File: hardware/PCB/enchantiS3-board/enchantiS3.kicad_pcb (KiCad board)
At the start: 4 copper layers, 55.9 x 25.4 mm, 66 parts, among them J1 USB_C_Receptacle_USB2.0, Q1 BSS138, Q2 BSS138, Q3 BSS138, SW1 B3U-1000P, SW2 B3U-1000P, U1 USBLC6-2P6, U2 MCP73871, U3 NCP167AMX330TBG, U4 NCP167AMX180TBG

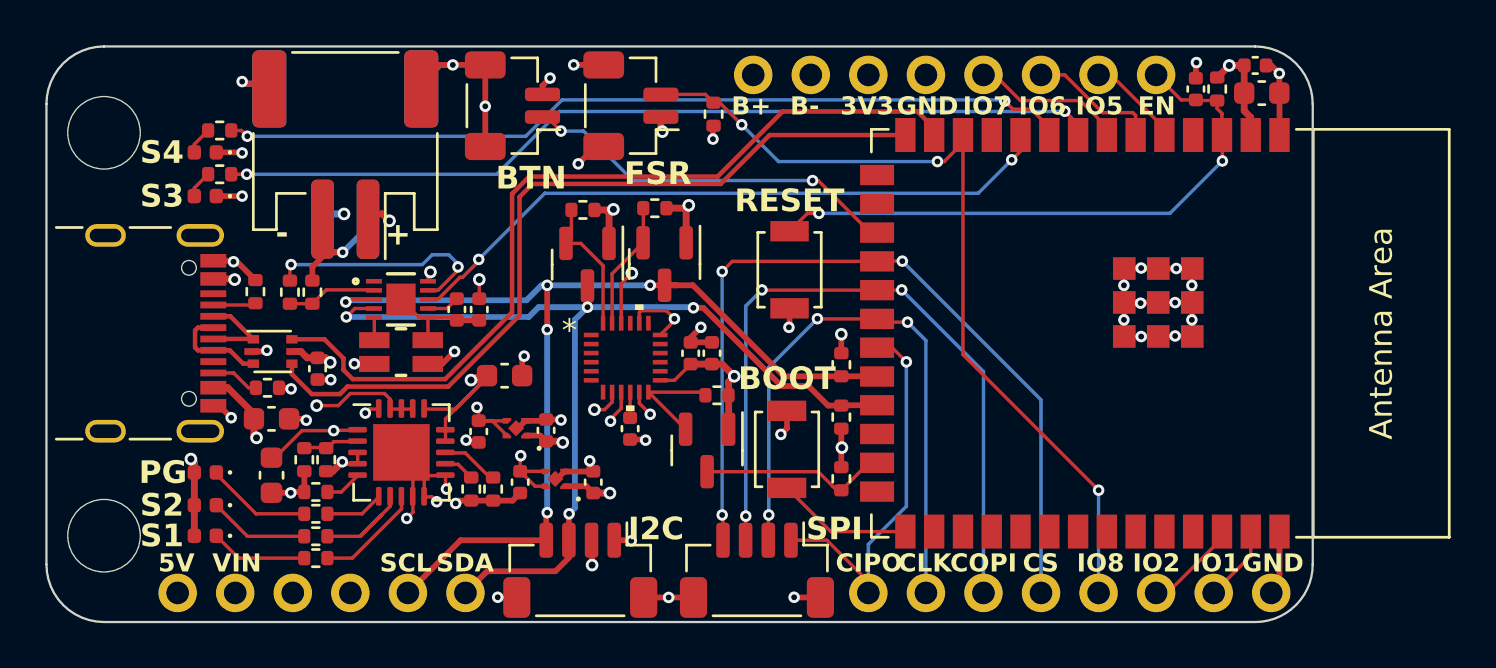
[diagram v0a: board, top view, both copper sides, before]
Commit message: removed, neopixel library, added extra LDO for peripherals
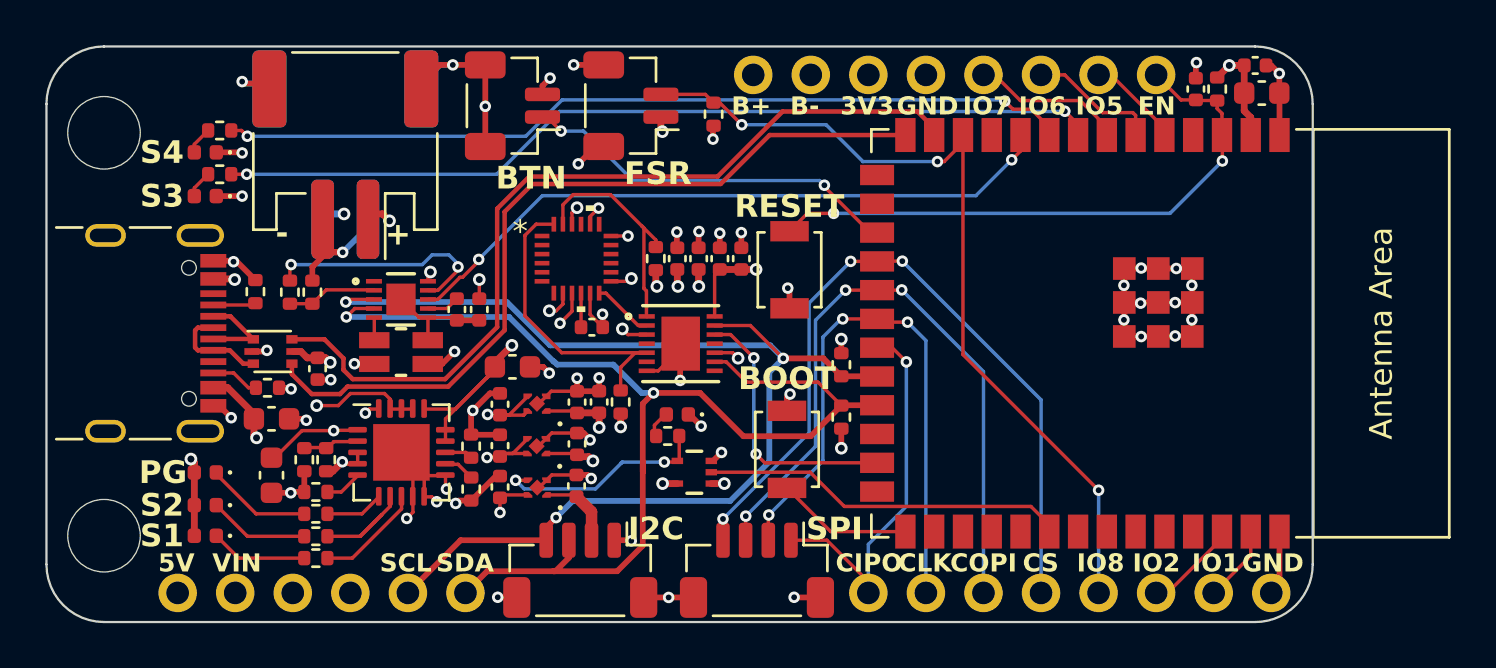
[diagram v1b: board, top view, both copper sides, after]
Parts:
- removed Q1, Q2, Q3: BSS138, Package_TO_SOT_SMD:SOT-23
- removed R21, R23: 2k2, Resistor_SMD:R_0402_1005Metric
- added C16: 1uF, Capacitor_SMD:C_0402_1005Metric, F.Cu at (116.1, 67.7)
- added C17: 1uF, Capacitor_SMD:C_0402_1005Metric, F.Cu at (112.7, 65.9)
- added C18: 0.1uF, Capacitor_SMD:C_0402_1005Metric, F.Cu at (117.1, 64.0)
- added C20: 1uF, Capacitor_SMD:C_0402_1005Metric, F.Cu at (122.4, 57.6)
- added C21: 0.1uF, Capacitor_SMD:C_0402_1005Metric, F.Cu at (123.4, 57.6)
- added LDOLED1: LDO2LED, LED_SMD:LED_0402_1005Metric, F.Cu at (120.5, 64.5)
- added R11: 1k, Resistor_SMD:R_0402_1005Metric, F.Cu at (120.1, 65.5)
- added U5: NCP167AMX330TBG, NCP167AMX330TBG-footprints:XDFN4_1X1_711AJ_ONS, F.Cu at (114.4, 67.7)
- added U6: NL17SV08XV5T2G, NL17SV08-footprints:SOT553-5_ONS, F.Cu at (121.3, 67.0)
- added U7: max3378eetd+t, MAX3378E-footprints:21-0137I_T1433-2_MXM, F.Cu at (120.7, 61.4)
- moved R15 8.64 mm to (118.0, 64.0), turned to -90 degrees
- moved IMU1 4.88 mm to (116.1, 57.6)
- moved C6 4.78 mm to (116.8, 60.6), turned to 0 degrees
- moved C10 4.22 mm to (121.5, 57.6)
- moved C7 4.22 mm to (120.5, 57.6)
- moved R14 2.23 mm to (119.6, 57.6), turned to -90 degrees
- moved R20 2.13 mm to (111.5, 65.9), turned to -90 degrees
- moved C12 1.85 mm to (116.1, 64.0)
- moved C5 1.83 mm to (116.1, 65.8)
- moved U3 1.66 mm to (114.3, 65.9)
- moved C11 1.53 mm to (112.7, 64.0), turned to 90 degrees
- moved U4 1.42 mm to (114.4, 64.0)
- moved C4 0.91 mm to (112.7, 67.7), turned to 90 degrees
- moved C8 0.52 mm to (113.3, 62.4)
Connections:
- TOUCH1 pad 2: +3V3 -> +3V3_AUX
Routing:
- net /IO39: track 0.00 -> 16.2 mm
- net GND: track 80.4 -> 92.3 mm, vias 48 -> 56
- net /LDO_EN: track 0.00 -> 9.56 mm, vias 0 -> 2
- net /SCL: track 45.6 -> 53.2 mm, vias 5 -> 3
- net /SDA: track 44.3 -> 51.7 mm, vias 4 -> 2
- net /LV_SDA: track 6.16 -> 13.5 mm
- net +1V8: track 16.9 -> 11.2 mm, vias 6 -> 10
- net /LV_SCL: track 5.64 -> 10.4 mm
- net /IO48: track 8.34 -> 11.9 mm, vias 0 -> 2
- net +3V3_AUX: track 0.00 -> 3.55 mm
- net /CS: track 37.2 -> 34.1 mm
- net +3V3: track 11.1 -> 14.0 mm, vias 6 -> 8
- net /IMU_INT: track 4.89 -> 2.69 mm
- net /COPI: track 32.4 -> 30.2 mm
- net SYS: track 11.3 -> 13.0 mm, vias 4 -> 5
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
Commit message: updated schematic
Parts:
- removed LDOLED1: LDO2LED, LED_SMD:LED_0402_1005Metric
- removed R11: 1k, Resistor_SMD:R_0402_1005Metric
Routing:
- net /SDA: track 51.7 -> 50.4 mm
- net /LDO_EN: track 9.56 -> 8.33 mm
- net Net-(LDOLED1-A): track 1.22 -> 0.00 mm
- net GND: track 92.3 -> 91.5 mm, vias 56 -> 55

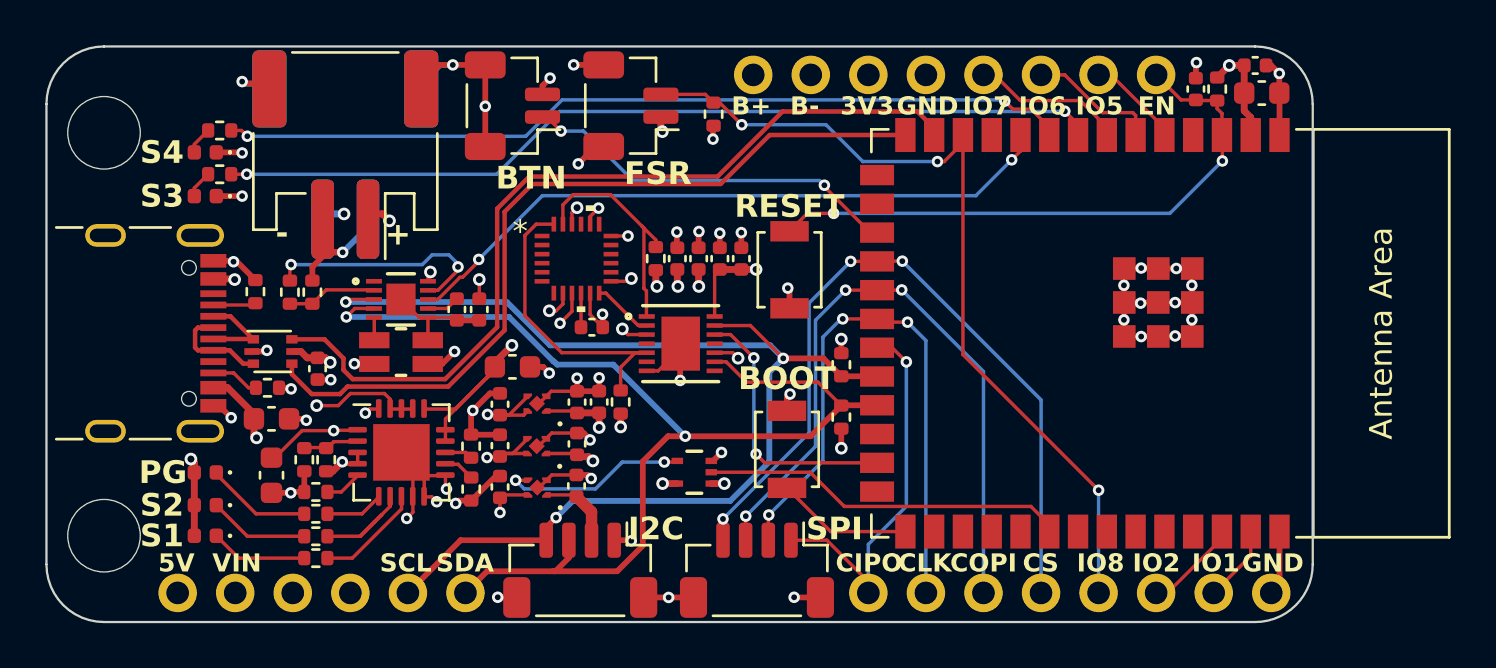
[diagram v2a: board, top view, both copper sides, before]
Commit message: upadated schematic, connected IMU data pins to SPI line, updated manufacturing files
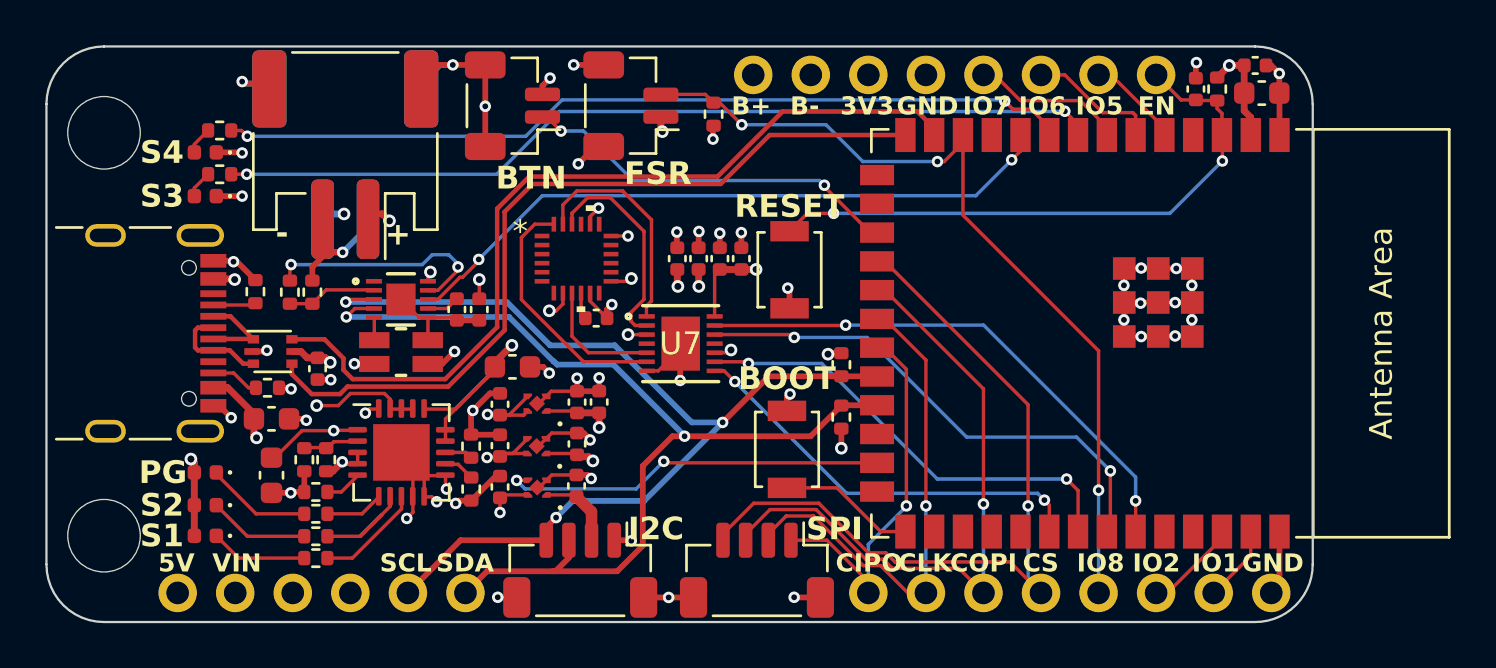
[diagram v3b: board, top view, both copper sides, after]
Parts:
- removed R14, R15: 2k2, Resistor_SMD:R_0402_1005Metric
- removed U6: NL17SV08XV5T2G, NL17SV08-footprints:SOT553-5_ONS
- moved C6 0.44 mm to (117.0, 60.2)
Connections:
- net /LV_SCL renamed /CLK_1V8
- IMU1 pad 12: /IMU_INT -> unconnected-(IMU1-INT1-Pad12)
- IMU1 pad 22: +1V8 -> /CS_1V8
- IMU1 pad 24: /LV_SDA -> /COPI_1V8
- IMU1 pad 9: GND -> /CIPO_1V8
- MCU1 pad 25: /IO48 -> /LDO_EN
- MCU1 pad 32: /IO39 -> /COPI_AUX
- MCU1 pad 33: /IO40 -> /CIPO_AUX
- MCU1 pad 34: /IO41 -> /CS_AUX
- MCU1 pad 35: /IO42 -> /CLK_AUX
- U7 pad 12: /IO48 -> /CS_AUX
- U7 pad 13: /SCL -> /CLK_AUX
- U7 pad 2: /IMU_INT -> /CS_1V8
- U7 pad 5: /LV_SDA -> /CIPO_1V8
- U7 pad 6: unconnected-(U7-I/O_VL4-Pad6) -> /COPI_1V8
- U7 pad 8: unconnected-(U7-I/O_VCC4-Pad8) -> /COPI_AUX
- U7 pad 9: /SDA -> /CIPO_AUX
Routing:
- net /CLK_AUX: track 0.00 -> 23.8 mm, vias 0 -> 2
- net /CS_AUX: track 0.00 -> 22.7 mm, vias 0 -> 2
- net /CIPO_AUX: track 0.00 -> 20.2 mm, vias 0 -> 2
- net /COPI_AUX: track 0.00 -> 18.4 mm, vias 0 -> 2
- net /IO39: track 16.2 -> 0.00 mm
- net /LV_SDA: track 13.5 -> 0.00 mm
- net /IO48: track 11.9 -> 0.00 mm, vias 2 -> 0
- net /COPI_1V8: track 0.00 -> 11.1 mm
- net /CS_1V8: track 0.00 -> 9.54 mm
- net /LDO_EN: track 8.33 -> 17.1 mm
- net /SCL: track 53.2 -> 45.1 mm
- net /SDA: track 50.4 -> 43.9 mm
- net /CIPO_1V8: track 0.00 -> 5.50 mm
- net /SCLK: track 26.4 -> 22.1 mm, vias 3 -> 1
- net +1V8: track 11.2 -> 8.29 mm, vias 10 -> 7
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
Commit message: updated BOM and manufacturing files
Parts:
- R22, R3: value 1k -> 2k
- R24: value 1k -> 470
- moved C18 2.77 mm to (117.0, 61.2), turned to 180 degrees
- moved C10 1.87 mm to (119.7, 58.1)
- moved C7 1.87 mm to (118.8, 58.1)
- moved C20 0.98 mm to (122.4, 58.6)
- moved C21 0.98 mm to (123.4, 58.6)
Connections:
- U4 pad 3: SYS -> /LDO_EN
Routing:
- net /LDO_EN: track 17.1 -> 21.3 mm, vias 2 -> 3
- net SYS: track 13.0 -> 11.4 mm
- net /CS_1V8: track 9.54 -> 11.1 mm
- net /CIPO_1V8: track 5.50 -> 6.65 mm
- net /CLK_1V8: track 9.91 -> 11.0 mm
- net +3V3: track 12.7 -> 11.8 mm
- net +1V8: track 8.29 -> 8.64 mm, vias 7 -> 5
- net GND: track 89.2 -> 88.8 mm, vias 53 -> 51
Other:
- board text added: "EnchantiS3 v0.3 2024-02 IDMIL McGill University Albert Niyonsenga"
- board text removed: "EnchantiS3 v0.1 2023-12 IDMIL McGill University Albert Niyonsenga"
